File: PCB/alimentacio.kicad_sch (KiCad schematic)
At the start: 17 parts, among them J1 PowerIN, U1 LT1528CT-PBF

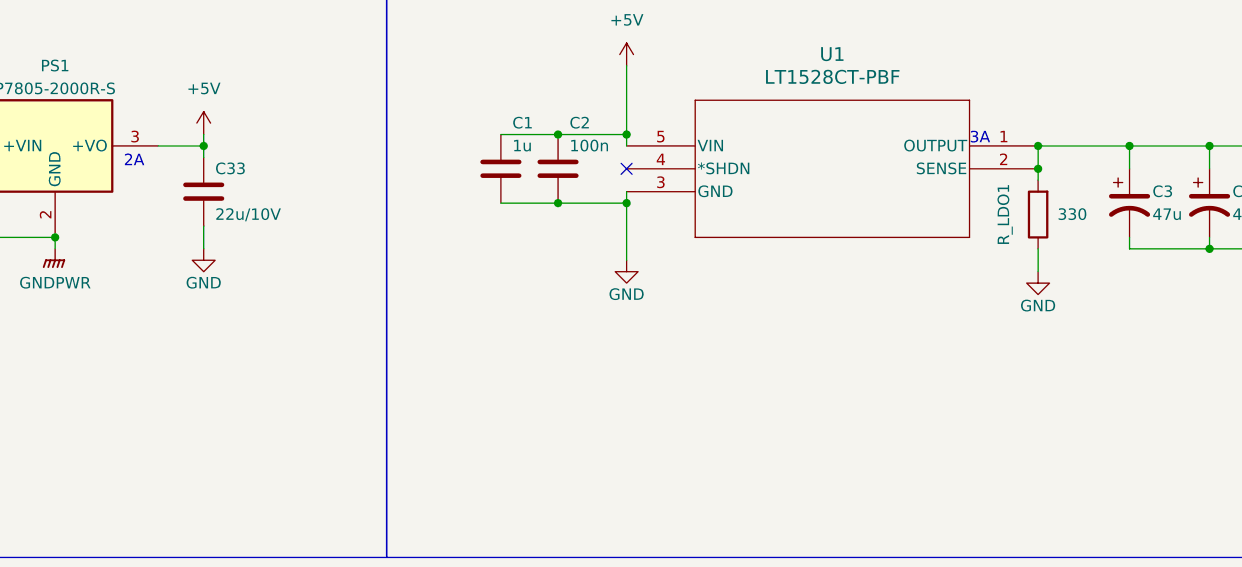
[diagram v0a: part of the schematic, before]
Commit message: Solució d'errors DRC
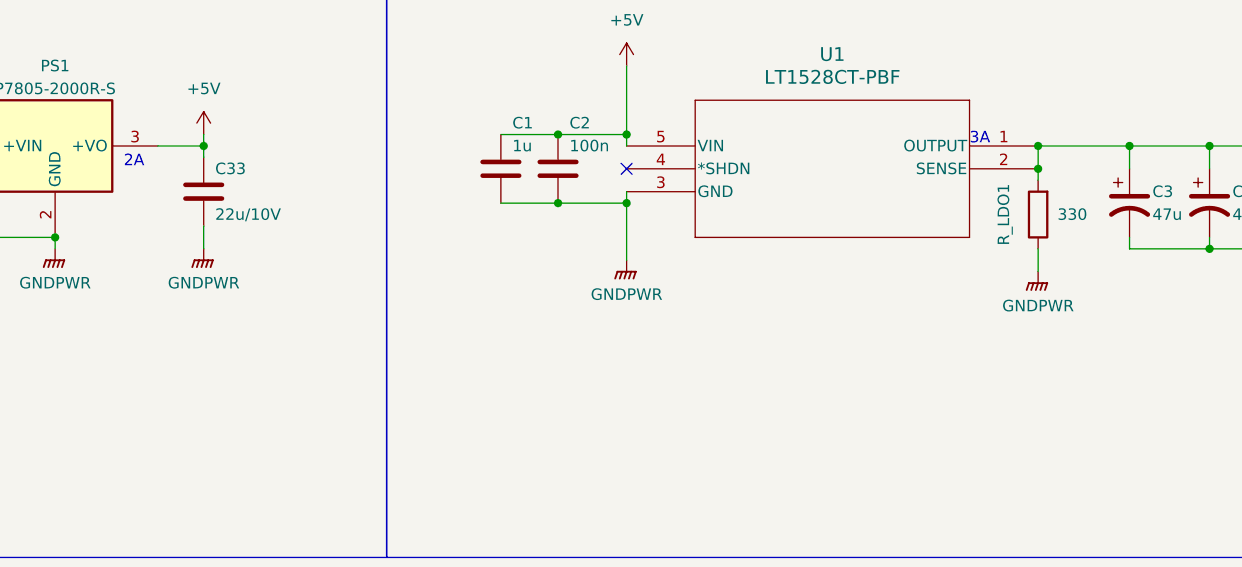
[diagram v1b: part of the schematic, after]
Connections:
- net GND: no longer C1.2, C2.2, C33.2, R_LDO1.1, U1.3 (GND)
- net GNDPWR: now also C1.2, C2.2, C33.2, R_LDO1.1, U1.3 (GND)
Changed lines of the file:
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@@
+    )
+  )
+  (symbol (lib_id "power:GNDPWR") (at 233.68 64.77 0) (unit 1)
+    (in_bom yes) (on_board yes) (dnp no)
+    (property "Reference" "#PWR057" (at 233.68 69.85 0)
+      (effects (font (size 1.27 1.27)) hide)
+    )
+    (property "Value" "GNDPWR" (at 233.68 68.58 0)
+      (effects (font (size 1.27 1.27)))
+    )
+    (property "Footprint" "" (at 233.68 66.04 0)
+      (effects (font (size 1.27 1.27)) hide)
+    )
+    (property "Datasheet" "" (at 233.68 66.04 0)
+      (effects (font (size 1.27 1.27)) hide)
+    )
+    (pin "1")
+    (instances
+      (project "DIJOUS_4_PORTES"
+        (path "/69b34976-047e-478e-bd76-9b6ef0dba356/0e58b9bb-7a32-4563-ae50-f5e325ba8348"
+          (reference "#PWR057") (unit 1)
+        )
+      )
     )
   )
@@
     )
   )
+  (symbol (lib_id "power:GNDPWR") (at 187.96 63.5 0) (unit 1)
+    (in_bom yes) (on_board yes) (dnp no)
+    (property "Reference" "#PWR08" (at 187.96 68.58 0)
+      (effects (font (size 1.27 1.27)) hide)
+    )
+    (property "Value" "GNDPWR" (at 187.96 67.31 0)
+      (effects (font (size 1.27 1.27)))
+    )
+    (property "Footprint" "" (at 187.96 64.77 0)
+      (effects (font (size 1.27 1.27)) hide)
+    )
+    (property "Datasheet" "" (at 187.96 64.77 0)
+      (effects (font (size 1.27 1.27)) hide)
+    )
+    (pin "1")
+    (instances
+      (project "DIJOUS_4_PORTES"
+        (path "/69b34976-047e-478e-bd76-9b6ef0dba356/0e58b9bb-7a32-4563-ae50-f5e325ba8348"
+          (reference "#PWR08") (unit 1)
+        )
+      )
+    )
+  )
   (symbol (lib_id "power:+3.3V") (at 270.51 41.91 0) (unit 1)
     (in_bom yes) (on_board yes) (dnp no) (fields_autoplaced)
@@
     )
   )
-  (symbol (lib_id "power:GND") (at 187.96 63.5 0) (unit 1)
-    (in_bom yes) (on_board yes) (dnp no)
-    (property "Reference" "#PWR059" (at 187.96 69.85 0)
-      (effects (font (size 1.27 1.27)) hide)
-    )
-    (property "Value" "GND" (at 187.96 67.31 0)
-      (effects (font (size 1.27 1.27)))
-    )
-    (property "Footprint" "" (at 187.96 63.5 0)
-      (effects (font (size 1.27 1.27)) hide)
-    )
-    (property "Datasheet" "" (at 187.96 63.5 0)
-      (effects (font (size 1.27 1.27)) hide)
-    )
-    (pin "1")
-    (instances
-      (project "DIJOUS_4_PORTES"
-        (path "/69b34976-047e-478e-bd76-9b6ef0dba356/0e58b9bb-7a32-4563-ae50-f5e325ba8348"
-          (reference "#PWR059") (unit 1)
-        )
-      )
-    )
-  )
   (symbol (lib_id "Device:C_Polarized_US") (at 261.62 57.15 0) (unit 1)
     (in_bom yes) (on_board yes) (dnp no)
@@
         (path "/88fa5da0-8701-4b36-a7b6-c9dab3428a53"
           (reference "#PWR055") (unit 1)
+        )
+      )
+    )
+  )
+  (symbol (lib_id "power:GNDPWR") (at 140.97 62.23 0) (unit 1)
+    (in_bom yes) (on_board yes) (dnp no)
+    (property "Reference" "#PWR07" (at 140.97 67.31 0)
+      (effects (font (size 1.27 1.27)) hide)
+    )
+    (property "Value" "GNDPWR" (at 140.97 66.04 0)
+      (effects (font (size 1.27 1.27)))
+    )
+    (property "Footprint" "" (at 140.97 63.5 0)
+      (effects (font (size 1.27 1.27)) hide)
+    )
+    (property "Datasheet" "" (at 140.97 63.5 0)
+      (effects (font (size 1.27 1.27)) hide)
+    )
+    (pin "1")
+    (instances
+      (project "DIJOUS_4_PORTES"
+        (path "/69b34976-047e-478e-bd76-9b6ef0dba356/0e58b9bb-7a32-4563-ae50-f5e325ba8348"
+          (reference "#PWR07") (unit 1)
         )
       )
@@
     )
   )
-  (symbol (lib_id "power:GND") (at 140.97 62.23 0) (unit 1)
-    (in_bom yes) (on_board yes) (dnp no)
-    (property "Reference" "#PWR07" (at 140.97 68.58 0)
-      (effects (font (size 1.27 1.27)) hide)
-    )
-    (property "Value" "GND" (at 140.97 66.04 0)
-      (effects (font (size 1.27 1.27)))
-    )
-    (property "Footprint" "" (at 140.97 62.23 0)
-      (effects (font (size 1.27 1.27)) hide)
-    )
-    (property "Datasheet" "" (at 140.97 62.23 0)
-      (effects (font (size 1.27 1.27)) hide)
-    )
-    (pin "1")
-    (instances
-      (project "DIJOUS_4_PORTES"
-        (path "/69b34976-047e-478e-bd76-9b6ef0dba356/0e58b9bb-7a32-4563-ae50-f5e325ba8348"
-          (reference "#PWR07") (unit 1)
-        )
-      )
-    )
-  )
   (symbol (lib_id "Device:D_Zener") (at 46.99 57.15 270) (unit 1)
     (in_bom yes) (on_board yes) (dnp no)
@@
         )
       )
-    )
-  )
-  (symbol (lib_id "power:GND") (at 233.68 64.77 0) (unit 1)
-    (in_bom yes) (on_board yes) (dnp no)
-    (property "Reference" "#PWR061" (at 233.68 71.12 0)
-      (effects (font (size 1.27 1.27)) hide)
-    )
-    (property "Value" "GND" (at 233.68 68.58 0)
-      (effects (font (size 1.27 1.27)))
-    )
-    (property "Footprint" "" (at 233.68 64.77 0)
-      (effects (font (size 1.27 1.27)) hide)
-    )
-    (property "Datasheet" "" (at 233.68 64.77 0)
-      (effects (font (size 1.27 1.27)) hide)
-    )
-    (pin "1")
-    (instances
-      (project "DIJOUS_4_PORTES"
-        (path "/69b34976-047e-478e-bd76-9b6ef0dba356/0e58b9bb-7a32-4563-ae50-f5e325ba8348"
-          (reference "#PWR061") (unit 1)
-        )
-      )

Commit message: PCB LAYOUT 2.0 - rearranged uc pins, changed smd Cs to ceramic
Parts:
- R1: footprint (none) -> Resistor_SMD:R_0805_2012Metric
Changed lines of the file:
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@@
       (effects (font (size 1.27 1.27)))
     )
-    (property "Footprint" "" (at 27.94 86.868 90)
+    (property "Footprint" "Resistor_SMD:R_0805_2012Metric" (at 27.94 86.868 90)
       (effects (font (size 1.27 1.27)) hide)
     )
